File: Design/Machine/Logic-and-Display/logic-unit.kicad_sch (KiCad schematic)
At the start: 22 parts, among them J2 RJ45, K1 SRD-12VDC-SL-C, K2 SRD-12VDC-SL-C, K3 SRD-12VDC-SL-C, K4 SRD-12VDC-SL-C, SW1 ToggleAutoPoints, SW2 SynchRemote, U4 ESP32_NODEMCU, U5 NRF24L01_Breakout, U6 5V in 7V out

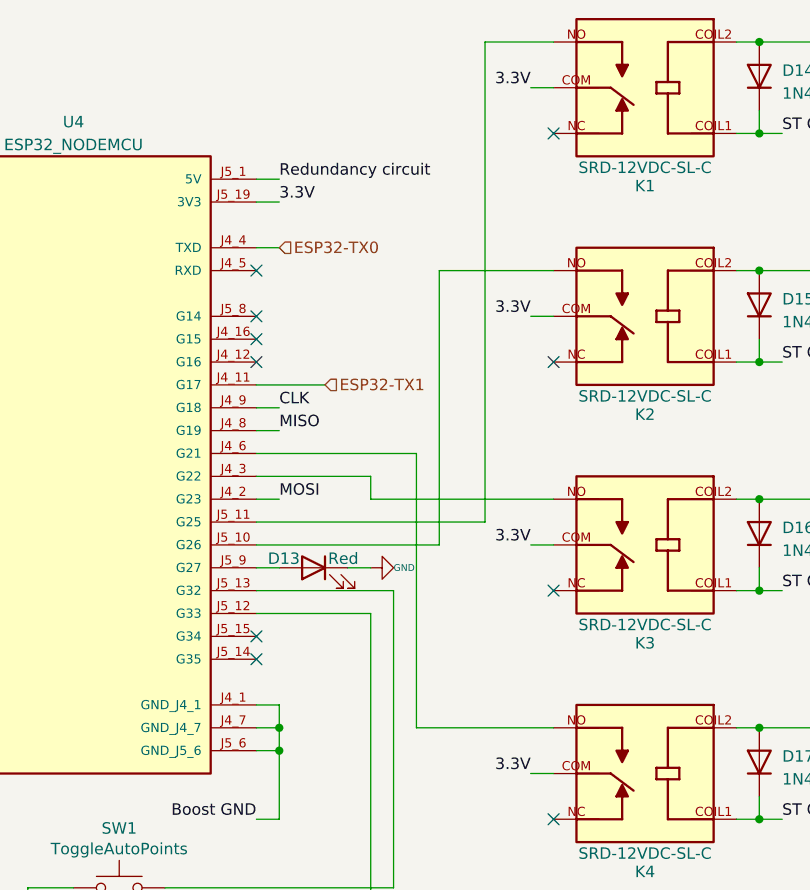
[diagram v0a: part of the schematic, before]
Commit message: fix: connections to st george 11 (#148)
fix connections to st george 11, RJ45's cables 1 and 3 are for right side (green), not left (red)
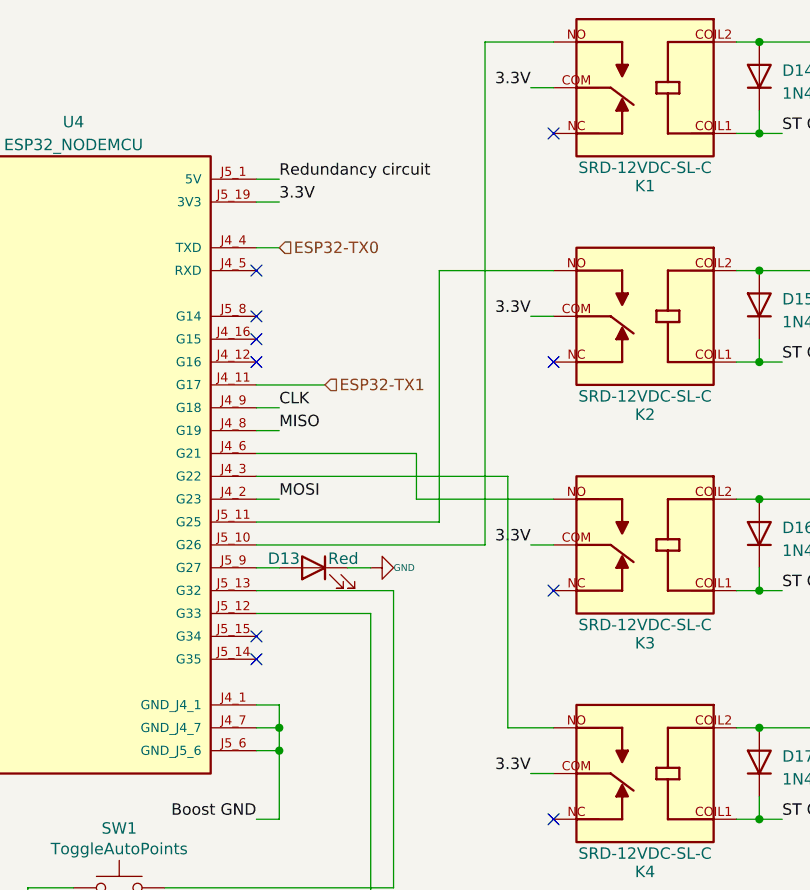
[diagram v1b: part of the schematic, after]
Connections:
- net at K1.NO: now also U4.J5_10 (G26); no longer U4.J5_11 (G25)
- net at K4.NO: now also U4.J4_3 (G22); no longer U4.J4_6 (G21)
- net at K3.NO: now also U4.J4_6 (G21); no longer U4.J4_3 (G22)
- net at K2.NO: now also U4.J5_11 (G25); no longer U4.J5_10 (G26)
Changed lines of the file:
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@@
-    (stroke (width 0) (type default))
-  )
-  (wire (pts (xy 71.12 91.44) (xy 96.52 91.44))
     (stroke (width 0) (type default))
   )
@@
     (stroke (width 0) (type default))
   )
-  (wire (pts (xy 88.9 114.3) (xy 88.9 83.82))
-    (stroke (width 0) (type default))
-  )
   (wire (pts (xy 114.3 152.4) (xy 104.14 152.4))
     (stroke (width 0) (type default))
@@
     (stroke (width 0) (type default))
   )
-  (wire (pts (xy 88.9 83.82) (xy 71.12 83.82))
-    (stroke (width 0) (type default))
-  )
-  (wire (pts (xy 91.44 93.98) (xy 71.12 93.98))
-    (stroke (width 0) (type default))
-  )
   (wire (pts (xy 124.46 63.5) (xy 127 63.5))
     (stroke (width 0) (type default))
@@
     (stroke (width 0) (type default))
   )
-  (wire (pts (xy 83.82 86.36) (xy 71.12 86.36))
-    (stroke (width 0) (type default))
-  )
   (wire (pts (xy 45.72 137.16) (xy 43.18 137.16))
     (stroke (width 0) (type default))
@@
     (stroke (width 0) (type default))
   )
-  (wire (pts (xy 83.82 86.36) (xy 83.82 88.9))
-    (stroke (width 0) (type default))
-  )
   (wire (pts (xy 167.64 38.1) (xy 127 38.1))
     (stroke (width 0) (type default))
   )
+  (wire (pts (xy 91.44 63.5) (xy 91.44 91.44))
+    (stroke (width 0) (type default))
+  )
   (wire (pts (xy 114.3 154.94) (xy 104.14 154.94))
     (stroke (width 0) (type default))
@@
     (stroke (width 0) (type default))
   )
+  (wire (pts (xy 99.06 86.36) (xy 71.12 86.36))
+    (stroke (width 0) (type default))
+  )
   (wire (pts (xy 104.14 153.67) (xy 100.33 153.67))
     (stroke (width 0) (type default))
@@
     (stroke (width 0) (type default))
   )
+  (wire (pts (xy 71.12 83.82) (xy 88.9 83.82))
+    (stroke (width 0) (type default))
+  )
   (wire (pts (xy 255.27 57.15) (xy 264.16 57.15))
     (stroke (width 0) (type default))
@@
     (stroke (width 0) (type default))
   )
-  (wire (pts (xy 91.44 63.5) (xy 91.44 93.98))
-    (stroke (width 0) (type default))
-  )
   (wire (pts (xy 218.44 78.74) (xy 220.98 78.74))
     (stroke (width 0) (type default))
@@
     (stroke (width 0) (type default))
   )
-  (wire (pts (xy 96.52 38.1) (xy 96.52 91.44))
+  (wire (pts (xy 96.52 38.1) (xy 96.52 93.98))
     (stroke (width 0) (type default))
   )
@@
     (stroke (width 0) (type default))
   )
-  (wire (pts (xy 83.82 88.9) (xy 104.14 88.9))
-    (stroke (width 0) (type default))
-  )
   (wire (pts (xy 83.82 101.6) (xy 83.82 142.24))
     (stroke (width 0) (type default))
@@
     (stroke (width 0) (type default))
   )
-  (wire (pts (xy 104.14 114.3) (xy 88.9 114.3))
+  (wire (pts (xy 104.14 114.3) (xy 99.06 114.3))
     (stroke (width 0) (type default))
   )
@@
     (stroke (width 0) (type default))
   )
+  (wire (pts (xy 104.14 88.9) (xy 88.9 88.9))
+    (stroke (width 0) (type default))
+  )
   (wire (pts (xy 111.76 170.18) (xy 87.63 170.18))
     (stroke (width 0) (type default))
   )
+  (wire (pts (xy 71.12 93.98) (xy 96.52 93.98))
+    (stroke (width 0) (type default))
+  )
   (wire (pts (xy 87.63 170.18) (xy 87.63 168.91))
     (stroke (width 0) (type default))
@@
     (stroke (width 0) (type default))
   )
+  (wire (pts (xy 99.06 114.3) (xy 99.06 86.36))
+    (stroke (width 0) (type default))
+  )
+  (wire (pts (xy 71.12 91.44) (xy 91.44 91.44))
+    (stroke (width 0) (type default))
+  )
+  (wire (pts (xy 88.9 88.9) (xy 88.9 83.82))
+    (stroke (width 0) (type default))
+  )
